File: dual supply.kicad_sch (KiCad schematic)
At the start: 32 parts, among them J6 703W-00/08, T1 VPP28–090, U1 X9C103S, U2 LM337_TO220, U3 X9C103S, U4 LM317T, U5 LM7805_TO220, U8 LM3940

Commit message: dodat tekst
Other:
- note added: "cimeru mojj"
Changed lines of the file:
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@@
     (effects (font (size 2.54 2.54) bold) (justify left bottom))
+  )
+  (text "cimeru mojj\n" (at 186.69 254.762 0)
+    (effects (font (size 1.27 1.27)) (justify left bottom))
   )
   (text "+5V" (at 285.75 34.925 0)

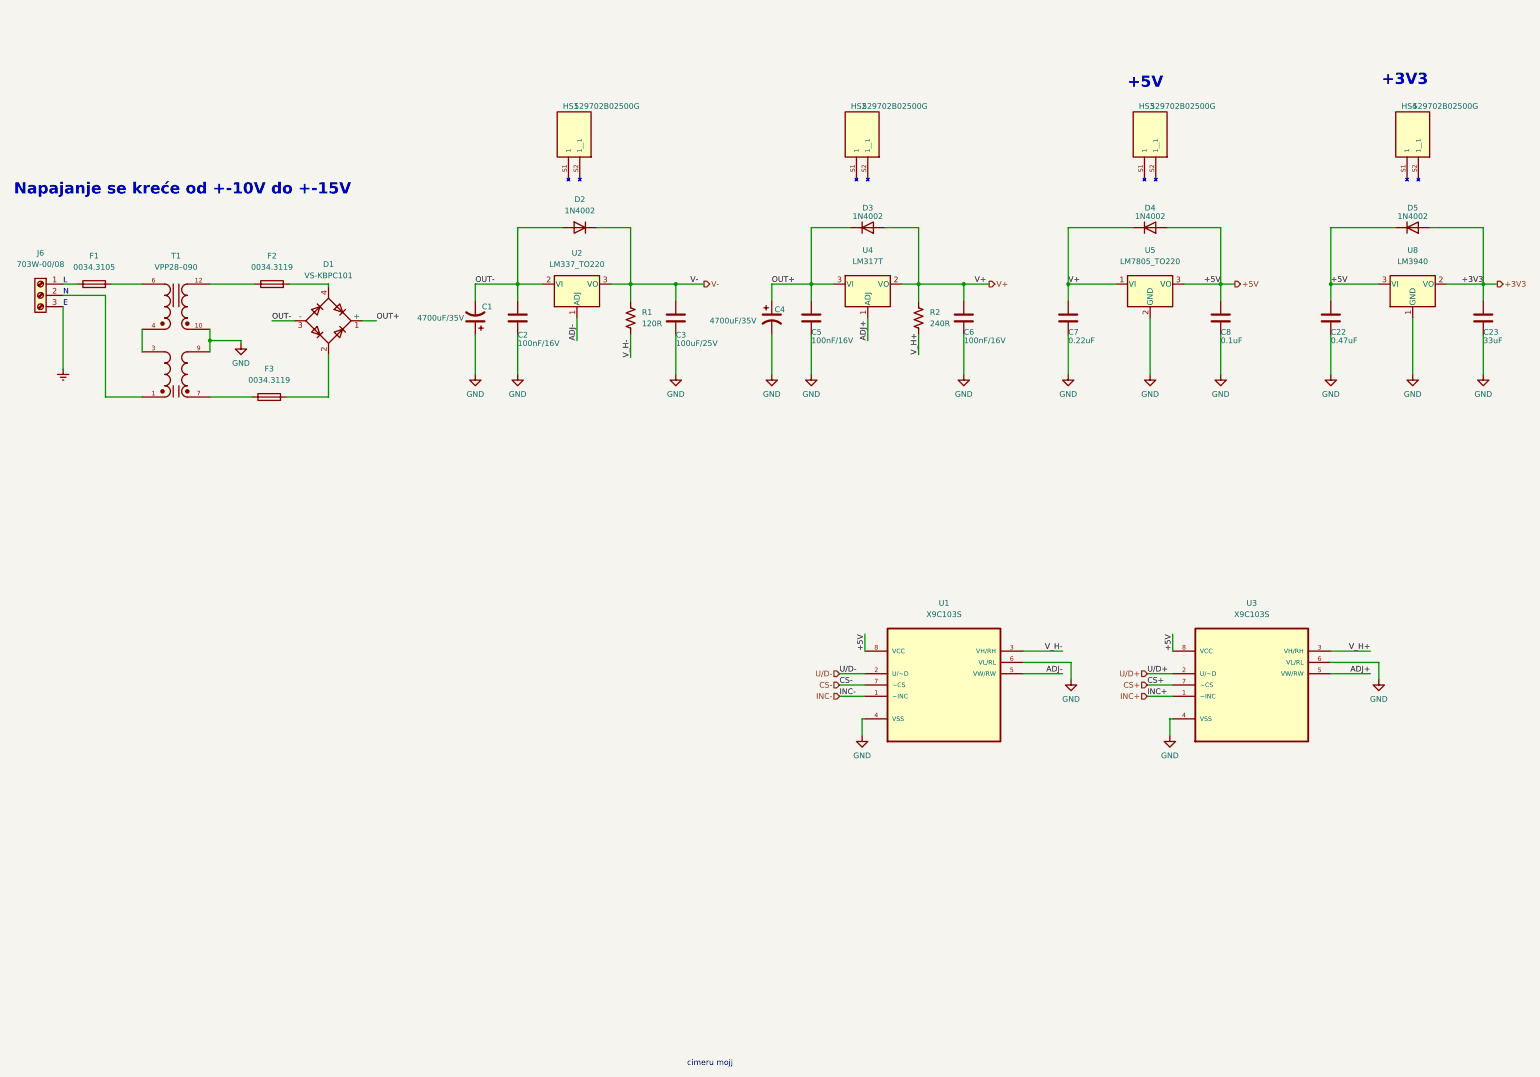
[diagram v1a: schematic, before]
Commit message: Simetricno postavljeni regulatori LM337 i LM317, labele V_- i V_+ su obrisane i digitalni potenciometri su vezani direktno za otpornike
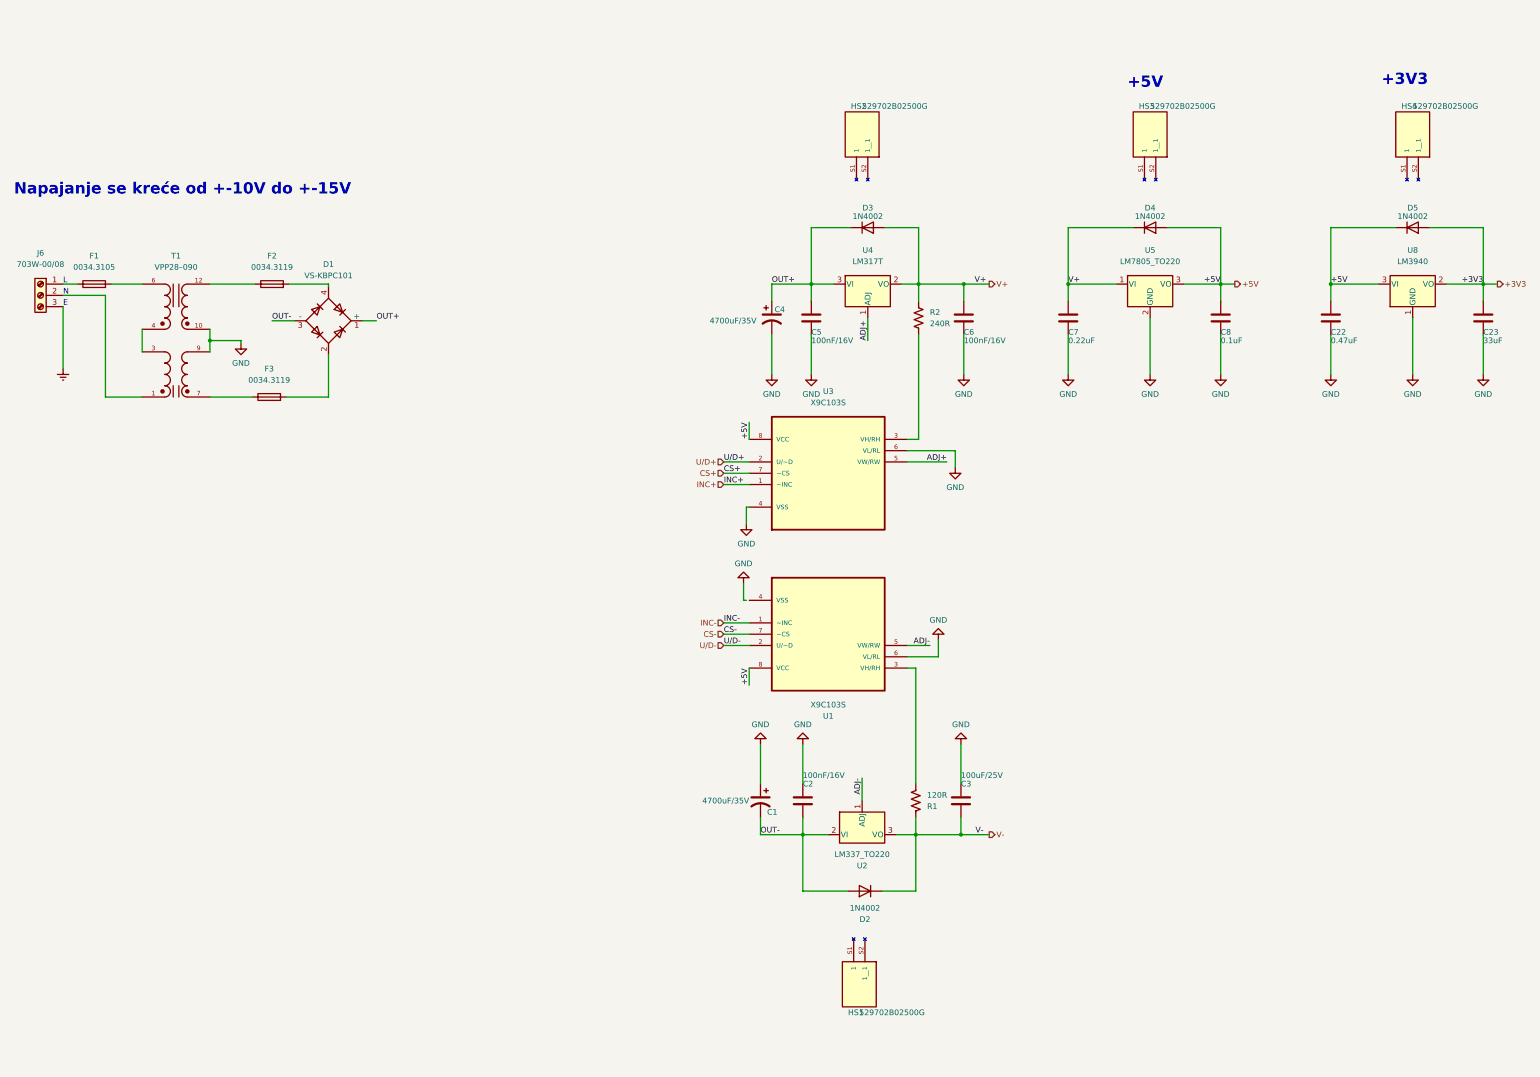
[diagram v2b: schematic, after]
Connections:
- net GND: no longer U1.4 (VSS)
- net V_H+: no longer names the net of R2.2, U3.3 (VH/RH)
- net V_H-: no longer names the net of R1.2, U1.3 (VH/RH)
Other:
- note removed: "cimeru mojj"
- moved on the sheet: C1, C2, C3, D2, HS1, R1, U1, U2, U3

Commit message: Promenjen je bypass kondenzator na LM317-T, umesto 100nF/16V sada stoji 100uF/25V.
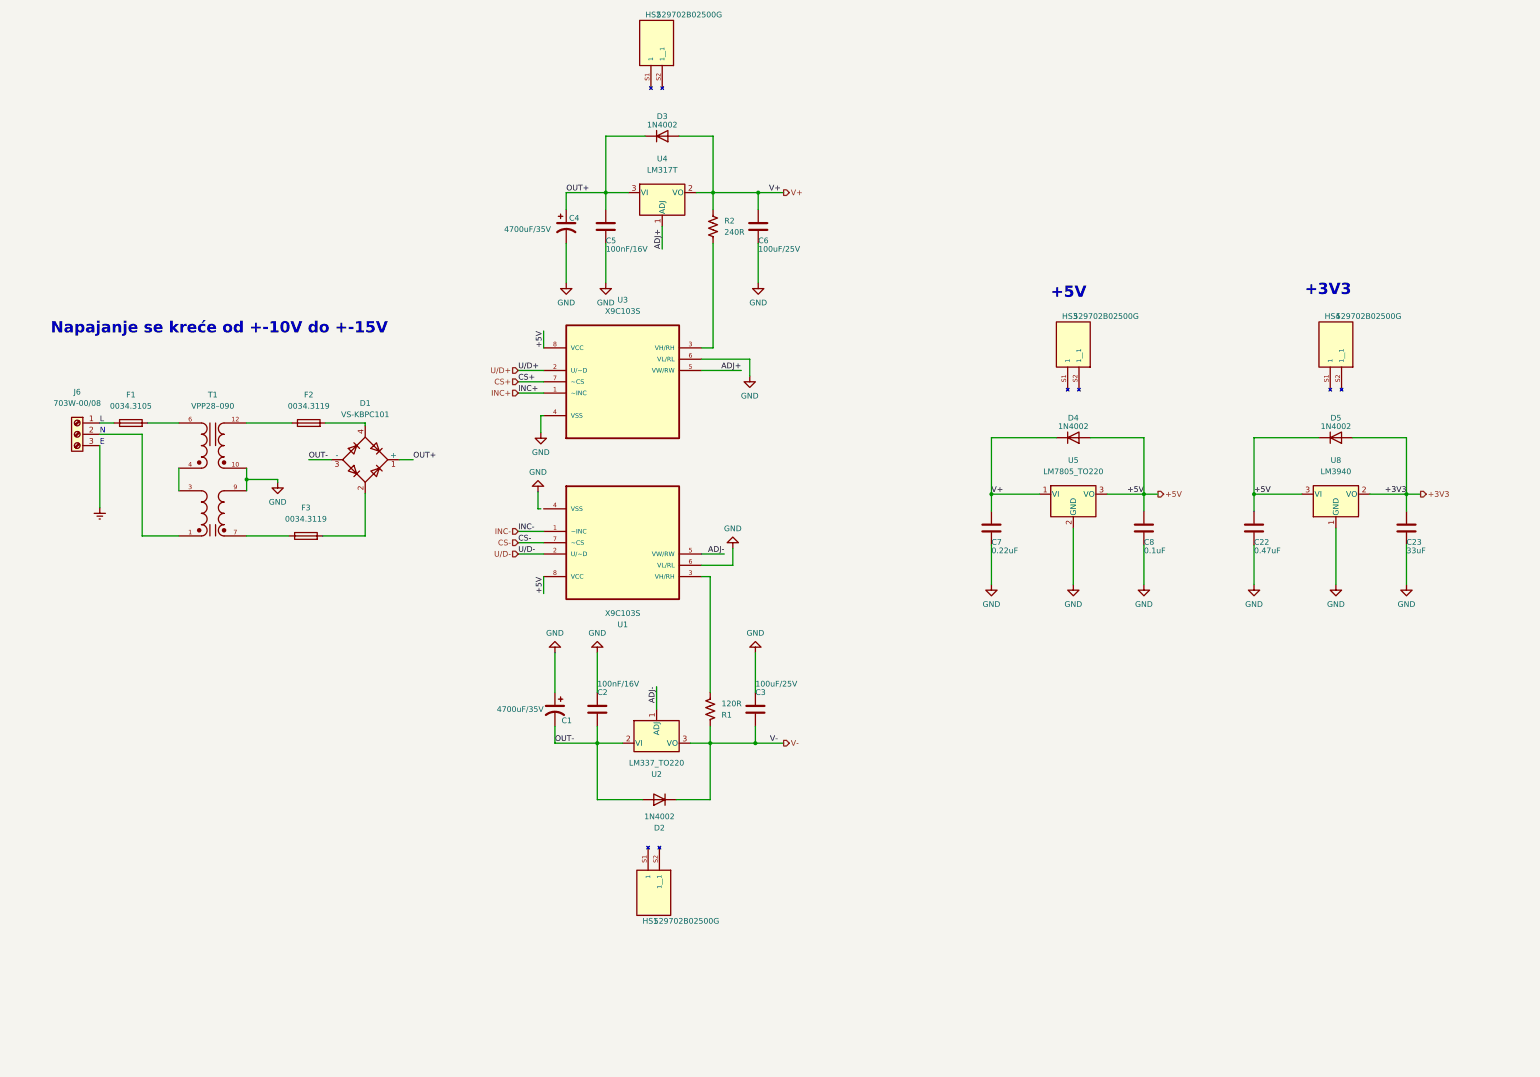
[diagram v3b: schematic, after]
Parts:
- C6: value 100nF/16V -> 100uF/25V
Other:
- moved on the sheet: C1, C2, C22, C23, C3, C4, C5, C6, C7, C8, D1, D2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

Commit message: dodat  buffer
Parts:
- added U?: AD8561, symbol Comparator:AD8561
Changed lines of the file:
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@@
     (pin "1")
+  )
+  (symbol (lib_id "Comparator:AD8561") (at 257.81 173.355 0) (unit 1)
+    (in_bom yes) (on_board yes) (fields_autoplaced)
+    (property "Reference" "U?" (id 0) (at 267.97 164.2362 0))
+    (property "Value" "AD8561" (id 1) (at 267.97 166.7762 0))
+    (property "Footprint" "" (id 2) (at 257.81 173.355 0)
+      (effects (font (size 1.27 1.27)) hide)
+    )
+    (property "Datasheet" "https://www.analog.com/media/en/technical-documentation/data-sheets/ad8561.pdf" (id 3) (at 257.81 173.355 0)
+      (effects (font (size 1.27 1.27)) hide)
+    )
+    (pin "1")
+    (pin "2")
+    (pin "3")
+    (pin "4")
+    (pin "5")
+    (pin "6")
+    (pin "7")
+    (pin "8")
   )
   (symbol (lib_id "power:GND") (at 289.433 146.304 0) (unit 1)

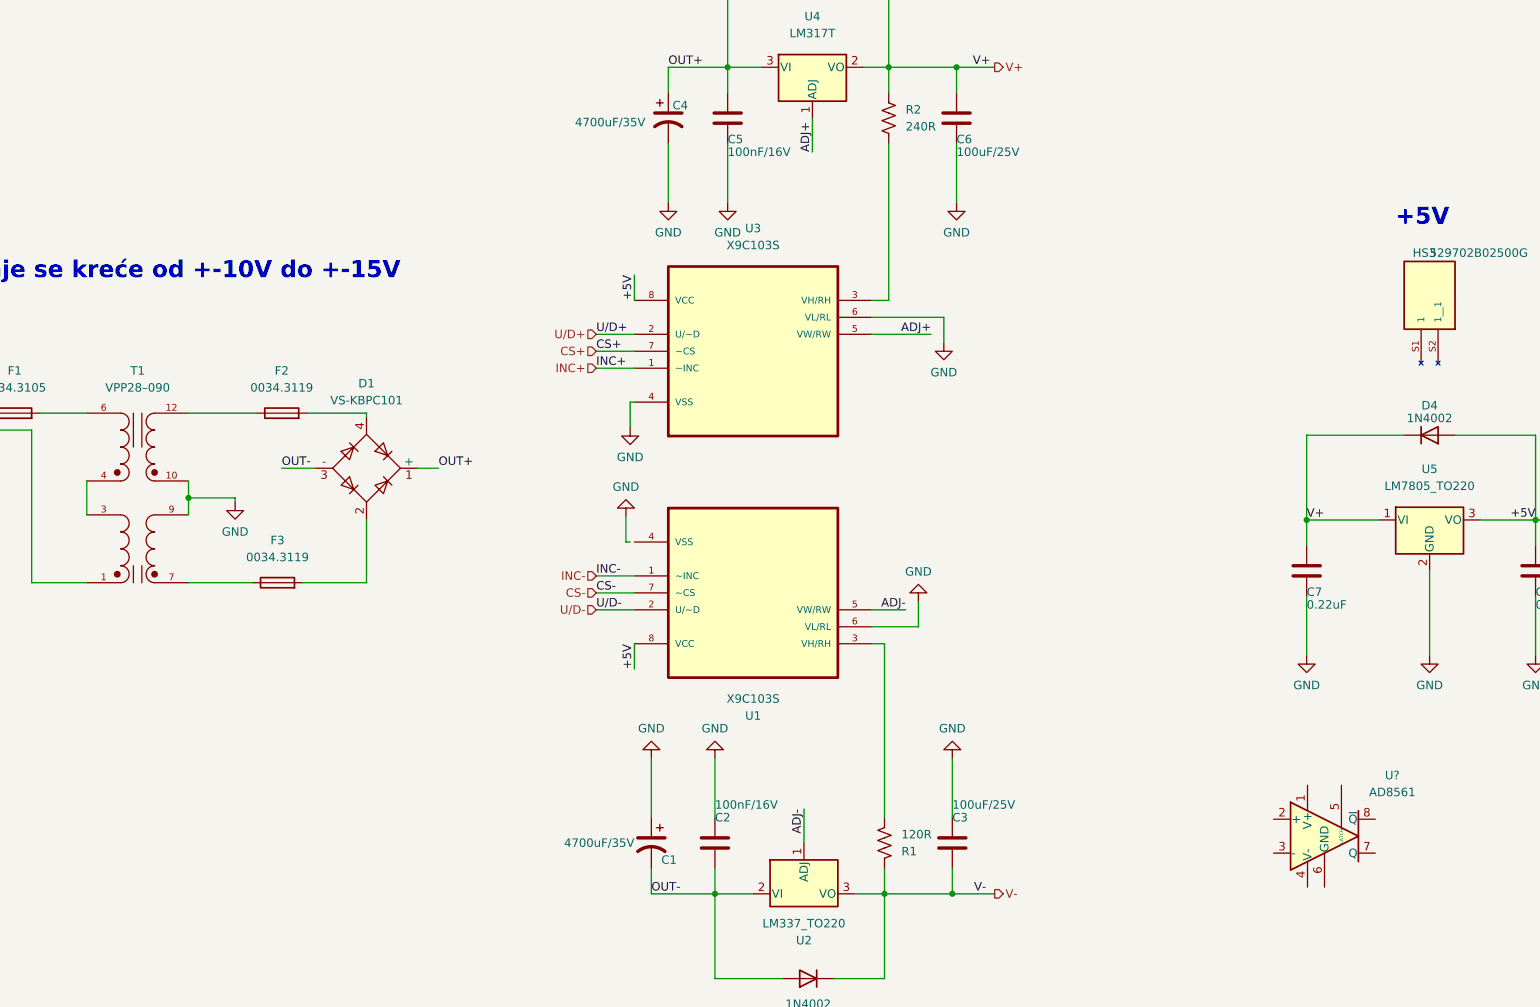
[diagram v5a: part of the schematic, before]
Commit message: Obrisan buffer
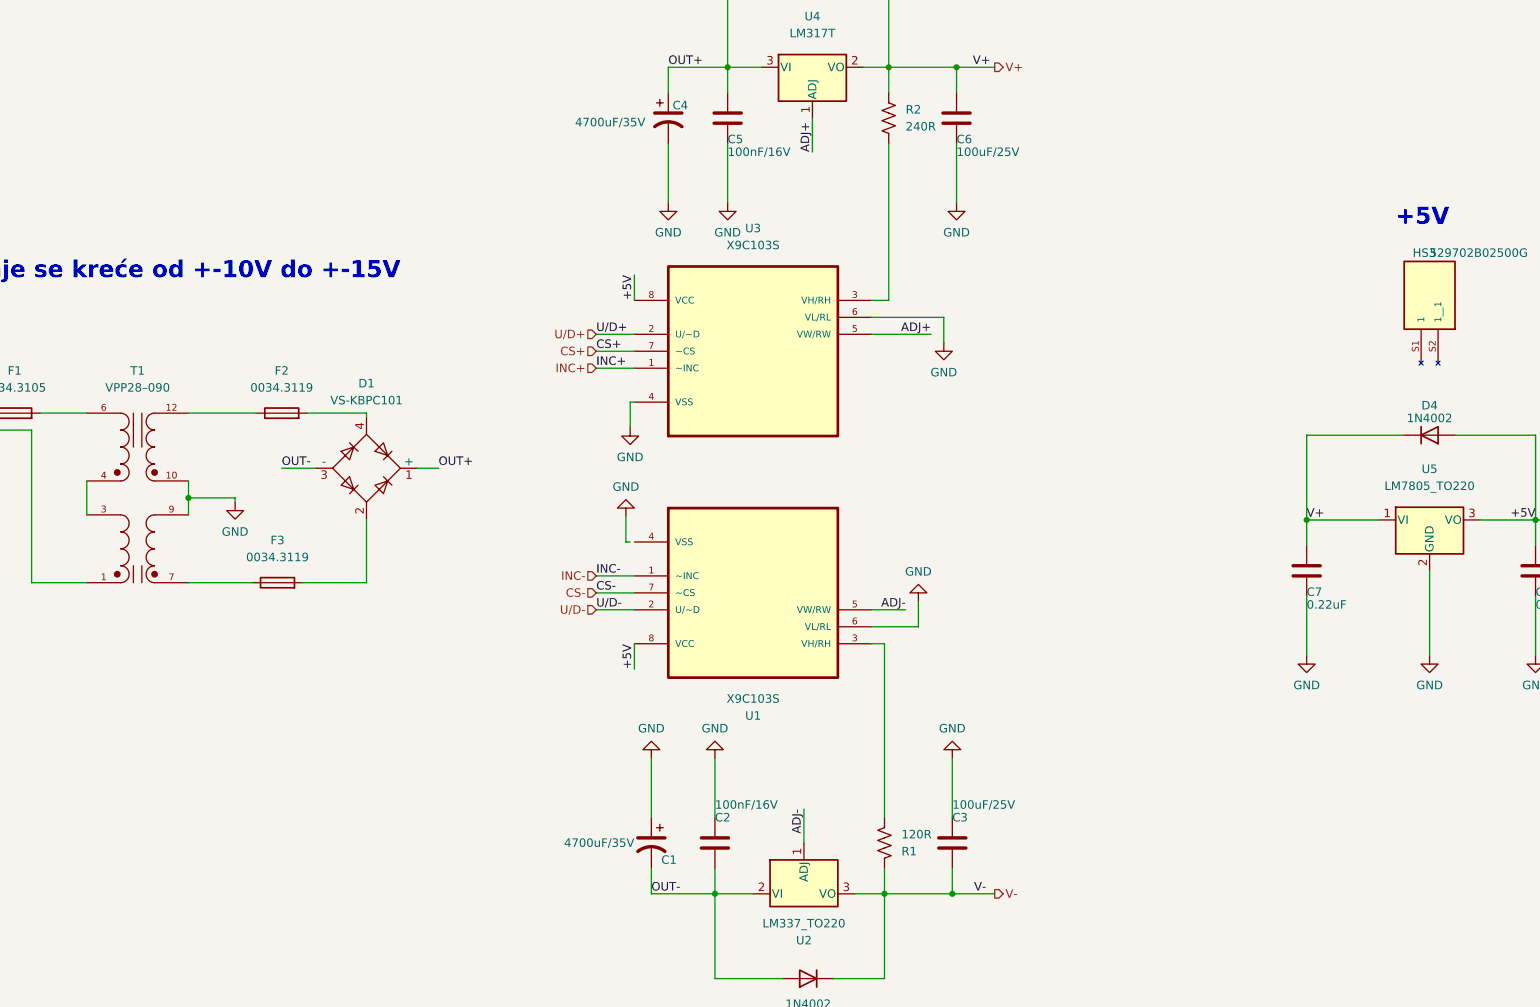
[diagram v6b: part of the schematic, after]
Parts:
- removed U?: AD8561, symbol Comparator:AD8561

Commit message: proba
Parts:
- added U?: AD8561, symbol Comparator:AD8561
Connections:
- new net: U?.3 (-), U?.7 (Q)

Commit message: obrisan buffer
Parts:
- removed U?: AD8561, symbol Comparator:AD8561
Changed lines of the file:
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@@
-    (stroke (width 0) (type default) (color 0 0 0 0))
-  )
-  (wire (pts (xy 250.19 175.895) (xy 250.19 182.245))
-    (stroke (width 0) (type default) (color 0 0 0 0))
-  )
-  (wire (pts (xy 262.89 177.8) (xy 265.43 177.8))
     (stroke (width 0) (type default) (color 0 0 0 0))
   )
@@
     (stroke (width 0) (type default) (color 0 0 0 0))
   )
-  (wire (pts (xy 262.89 182.245) (xy 262.89 177.8))
-    (stroke (width 0) (type default) (color 0 0 0 0))
-  )
   (wire (pts (xy 159.512 69.596) (xy 159.512 78.486))
     (stroke (width 0) (type default) (color 0 0 0 0))
@@
     (stroke (width 0) (type default) (color 0 0 0 0))
   )
-  (wire (pts (xy 250.19 182.245) (xy 262.89 182.245))
-    (stroke (width 0) (type default) (color 0 0 0 0))
-  )
   (wire (pts (xy 64.135 112.522) (xy 54.61 112.522))
     (stroke (width 0) (type default) (color 0 0 0 0))
@@
   )
   (wire (pts (xy 348.488 125.984) (xy 340.233 125.984))
-    (stroke (width 0) (type default) (color 0 0 0 0))
-  )
-  (wire (pts (xy 265.43 175.895) (xy 265.43 177.8))
     (stroke (width 0) (type default) (color 0 0 0 0))
   )
@@
     (pin "1")
   )
-  (symbol (lib_id "Comparator:AD8561") (at 257.81 173.355 0) (unit 1)
-    (in_bom yes) (on_board yes) (fields_autoplaced)
-    (property "Reference" "U?" (id 0) (at 267.97 164.2362 0))
-    (property "Value" "AD8561" (id 1) (at 267.97 166.7762 0))
-    (property "Footprint" "" (id 2) (at 257.81 173.355 0)
-      (effects (font (size 1.27 1.27)) hide)
-    )
-    (property "Datasheet" "https://www.analog.com/media/en/technical-documentation/data-sheets/ad8561.pdf" (id 3) (at 257.81 173.355 0)
-      (effects (font (size 1.27 1.27)) hide)
-    )
-    (pin "1")
-    (pin "2")
-    (pin "3")
-    (pin "4")
-    (pin "5")
-    (pin "6")
-    (pin "7")
-    (pin "8")
-  )
   (symbol (lib_id "power:GND") (at 289.433 146.304 0) (unit 1)
